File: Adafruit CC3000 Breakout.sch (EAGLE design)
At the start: 30 parts, among them U1 CC3000MOD, U3 74HC4050D, X1 2500AT44M0400E

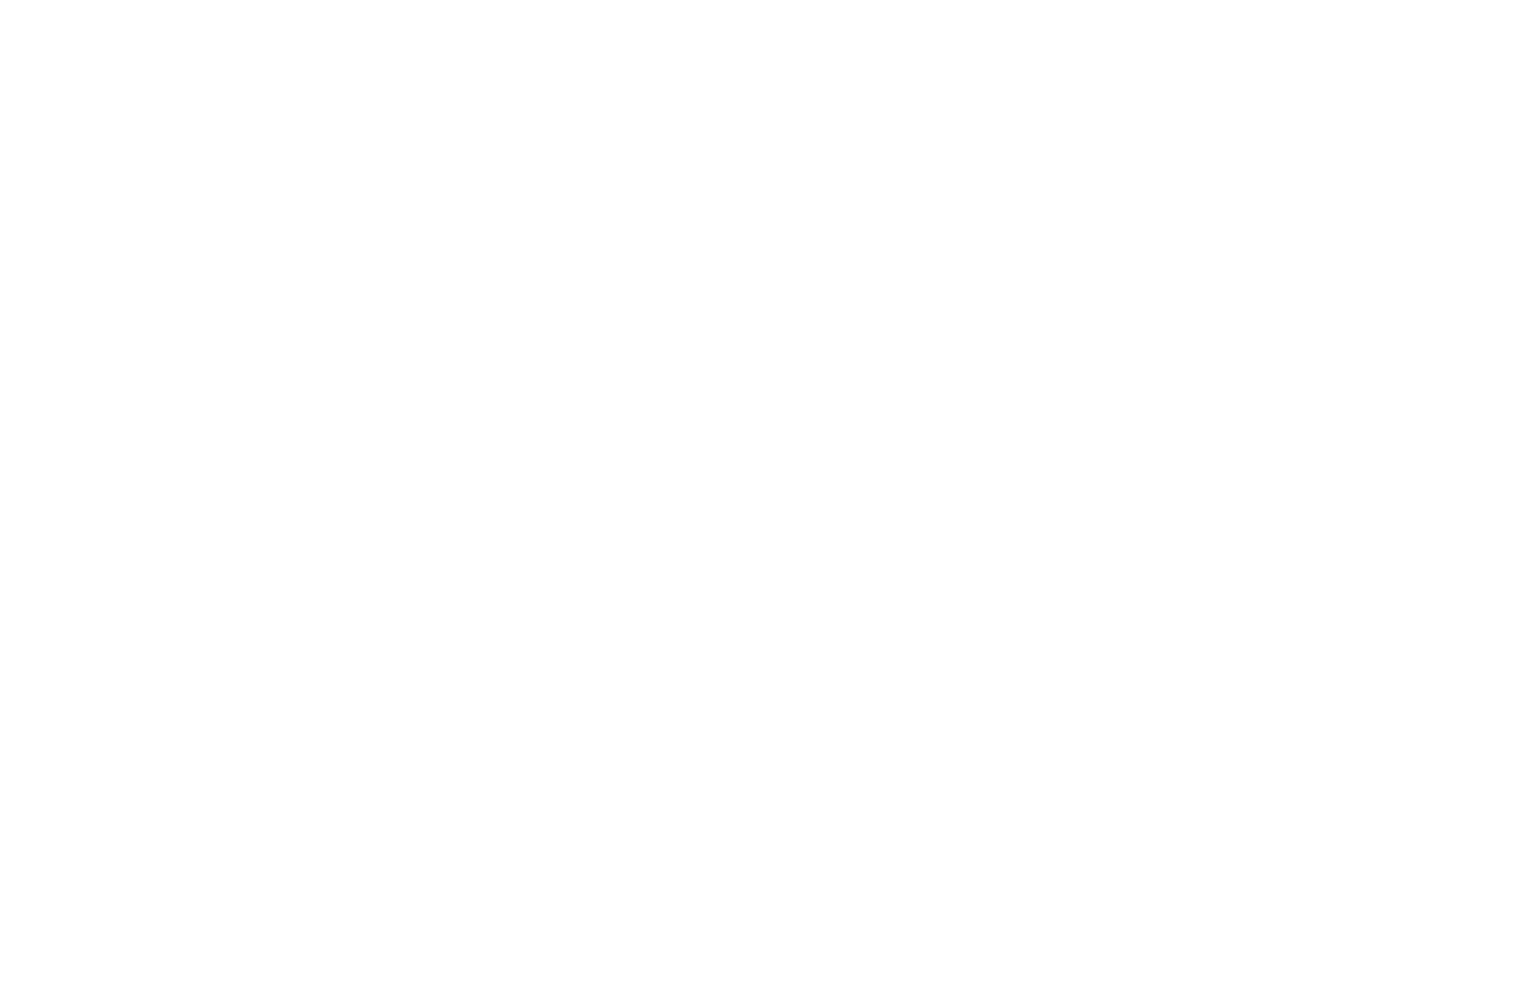
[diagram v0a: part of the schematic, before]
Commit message: Merge with net widget.
https://github.com/damellis/netwidget
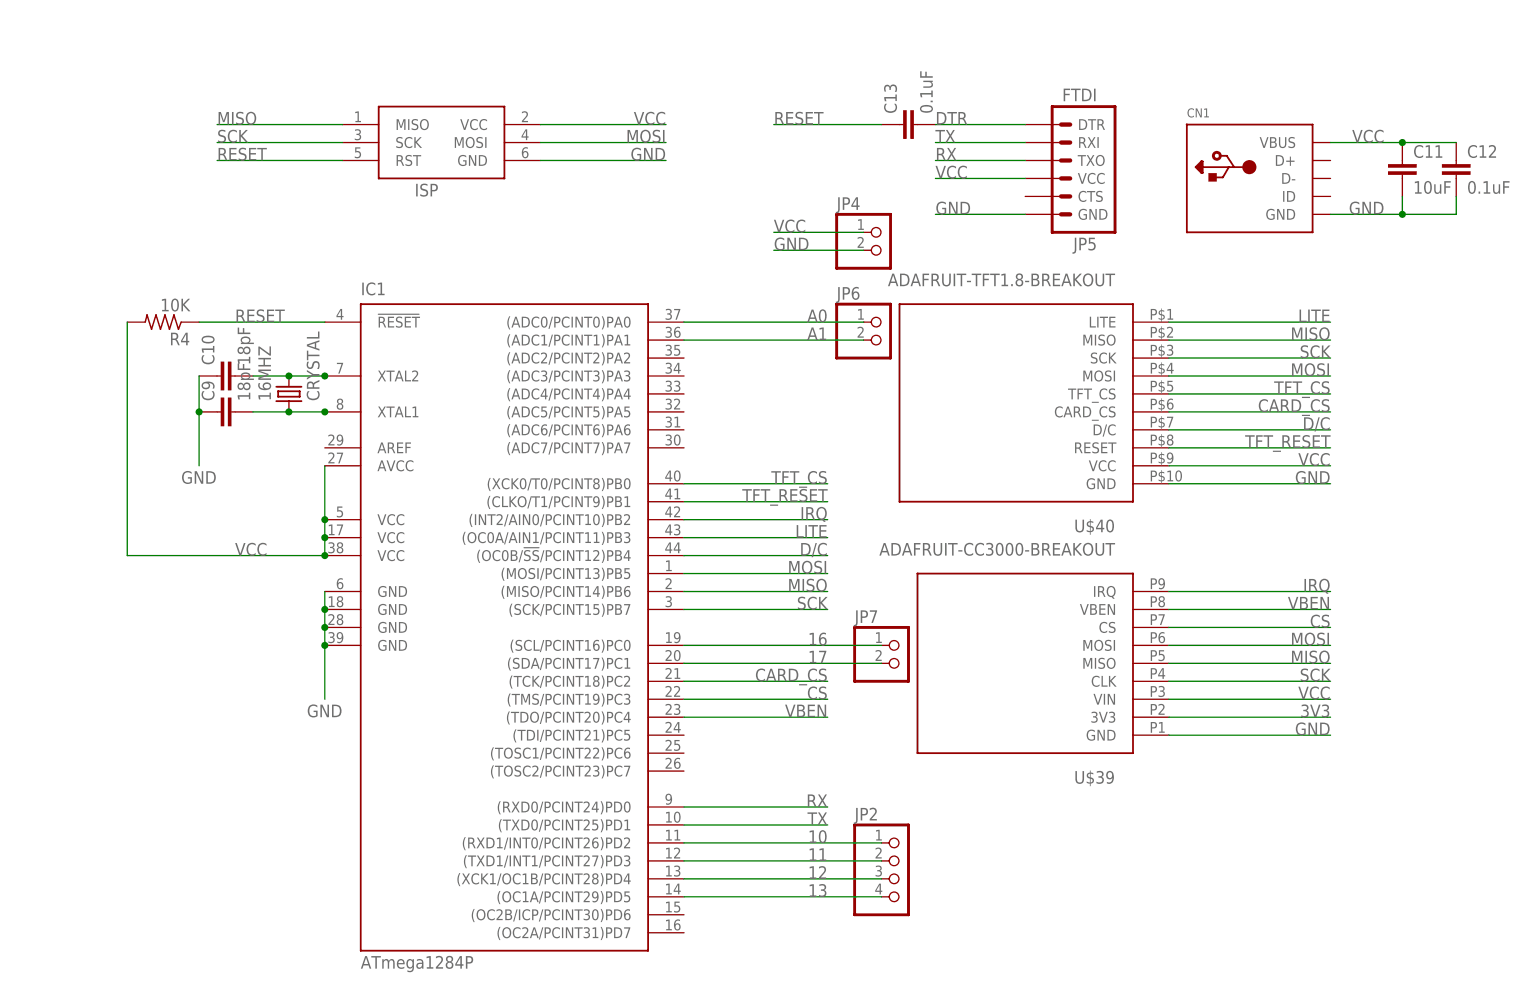
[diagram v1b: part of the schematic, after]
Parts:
- added 16MHZ: CRYSTAL, Net Widget:CRYSTAL
- added C10, C9: 18pF, rcl:C-EUC1206
- added C11: 10uF, rcl:C-EUC1206
- added C12, C13: 0.1uF, rcl:C-EUC1206
- added CN1: (no value), Net Widget:USBPWR
- added IC1: ATmega1284P, avr-5:MEGA164P/324P/644P-AU
- added ISP: AVRISP-6, adafruit:AVRISP-6
- added JP2: (no value), pinhead:PINHD-1X4
- added JP4, JP6, JP7: (no value), pinhead:PINHD-1X2
- added JP5: FTDI, Net Widget:ARDUINO_SERIAL_PROGRAMPTH
- added R4: 10K, rcl:R-US_R1206
- added U$39: ADAFRUIT-CC3000-BREAKOUT, Net Widget:ADAFRUIT-CC3000-BREAKOUT
- added U$40: ADAFRUIT-TFT1.8-BREAKOUT, Net Widget:ADAFRUIT-TFT1.8-BREAKOUT
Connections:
- new net 10: IC1.(RXD1/INT0/PCINT26)PD2, JP2.1
- new net 11: IC1.(TXD1/INT1/PCINT27)PD3, JP2.2
- new net 12: IC1.(XCK1/OC1B/PCINT28)PD4, JP2.3
- new net 13: IC1.(OC1A/PCINT29)PD5, JP2.4
- new net 16: IC1.(SCL/PCINT16)PC0, JP7.1
- new net 17: IC1.(SDA/PCINT17)PC1, JP7.2
- new net 3V3: U$39.3V3
- new net A0: IC1.(ADC0/PCINT0)PA0, JP6.1
- new net A1: IC1.(ADC1/PCINT1)PA1, JP6.2
- new net CARD_CS: IC1.(TCK/PCINT18)PC2, U$40.CARD_CS
- new net CS: IC1.(TMS/PCINT19)PC3, U$39.CS
- new net D/C: IC1.(OC0B/!SS!/PCINT12)PB4, U$40.D/C
- new net DTR: C13.2, JP5.DTR
- new net IRQ: IC1.(INT2/AIN0/PCINT10)PB2, U$39.IRQ
- new net LITE: IC1.(OC0A/AIN1/PCINT11)PB3, U$40.LITE
- new net MISO: IC1.(MISO/PCINT14)PB6, ISP.MISO, U$39.MISO, U$40.MISO
- new net MOSI: IC1.(MOSI/PCINT13)PB5, ISP.MOSI, U$39.MOSI, U$40.MOSI
- new net N$10: 16MHZ.1, C9.2, IC1.XTAL1
- new net N$8: 16MHZ.2, C10.2, IC1.XTAL2
- new net RESET: C13.1, IC1.!RESET, ISP.RST, R4.1
- new net RX: IC1.(RXD0/PCINT24)PD0, JP5.TXO
- new net SCK: IC1.(SCK/PCINT15)PB7, ISP.SCK, U$39.CLK, U$40.SCK
- new net TFT_CS: IC1.(XCK0/T0/PCINT8)PB0, U$40.TFT_CS
- new net TFT_RESET: IC1.(CLKO/T1/PCINT9)PB1, U$40.RESET
- new net TX: IC1.(TXD0/PCINT25)PD1, JP5.RXI
- new net VBEN: IC1.(TDO/PCINT20)PC4, U$39.VBEN
- new net VCC: C11.1, C12.1, CN1.VBUS, IC1.AVCC, IC1.VCC@1, IC1.VCC@2, IC1.VCC@3, ISP.VCC, JP4.1, JP5.VCC, R4.2, U$39.VIN, U$40.VCC
- net GND: now also C10.1, C11.2, C12.2, C9.1, CN1.GND, IC1.GND@1, IC1.GND@2, IC1.GND@3, IC1.GND@4, ISP.GND, JP4.2, JP5.GND, U$39.GND, U$40.GND

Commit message: Smoosh everything together.
Not routed yet, and some passives are 1206 and others are 0805.
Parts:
- removed 16MHZ: CRYSTAL, Net Widget:CRYSTAL
- removed C12: 0.1uF, rcl:C-EUC1206
- removed JP2: (no value), pinhead:PINHD-1X4
- removed JP3: (no value), microbuilder:HEADER-1X970MIL
- removed JP4, JP6, JP7: (no value), pinhead:PINHD-1X2
- removed U$39: ADAFRUIT-CC3000-BREAKOUT, Net Widget:ADAFRUIT-CC3000-BREAKOUT
- removed U$40: ADAFRUIT-TFT1.8-BREAKOUT, Net Widget:ADAFRUIT-TFT1.8-BREAKOUT
- removed U3: 74HC4050D, microbuilder:74HC4050D
- added 8MHZ: CRYSTAL, Net Widget:CRYSTAL
- C11: value 10uF -> 0.1uF
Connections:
- removed net 3V3: U$39.3V3
- removed net CARD_CS: IC1.(TCK/PCINT18)PC2, U$40.CARD_CS
- removed net CS: IC1.(TMS/PCINT19)PC3, U$39.CS
- removed net D/C: IC1.(OC0B/!SS!/PCINT12)PB4, U$40.D/C
- removed net IRQ: IC1.(INT2/AIN0/PCINT10)PB2, U$39.IRQ
- removed net LITE: IC1.(OC0A/AIN1/PCINT11)PB3, U$40.LITE
- removed net MISO: IC1.(MISO/PCINT14)PB6, ISP.MISO, U$39.MISO, U$40.MISO
- removed net MOSI: IC1.(MOSI/PCINT13)PB5, ISP.MOSI, U$39.MOSI, U$40.MOSI
- removed net SCK: IC1.(SCK/PCINT15)PB7, ISP.SCK, U$39.CLK, U$40.SCK
- removed net SPI_CLK_5V: JP3.6, U3.4A
- removed net SPI_CS_5V: JP3.3, R3.2, U3.6A
- removed net SPI_MOSI_5V: JP3.4, U3.5A
- removed net TFT_CS: IC1.(XCK0/T0/PCINT8)PB0, U$40.TFT_CS
- removed net TFT_RESET: IC1.(CLKO/T1/PCINT9)PB1, U$40.RESET
- removed net VBAT_EN_5V: JP3.2, R2.2, U3.3A
- removed net VBEN: IC1.(TDO/PCINT20)PC4, U$39.VBEN
- removed net VCC: C11.1, C12.1, CN1.VBUS, IC1.AVCC, IC1.VCC@1, IC1.VCC@2, IC1.VCC@3, ISP.VCC, JP4.1, JP5.VCC, R4.2, U$39.VIN, U$40.VCC
- net 10: no longer JP2.1
- net 11: no longer JP2.2
- net 12: no longer JP2.3
- net 13: no longer JP2.4
- net 16: no longer JP7.1
- net 17: no longer JP7.2
- net A0: no longer JP6.1
- net A1: no longer JP6.2
- net GND: no longer C12.2, JP3.9, JP4.2, U$39.GND, U$40.GND, U3.GND
- net N$10: now also 8MHZ.1; no longer 16MHZ.1
- net N$8: now also 8MHZ.2; no longer 16MHZ.2
- net SPI_CLK_3V: now also IC1.(SCK/PCINT15)PB7, ISP.SCK; no longer U3.4Y
- net SPI_CS_3V: now also IC1.(TMS/PCINT19)PC3, R3.2; no longer U3.6Y
- net SPI_IRQ_3V: now also IC1.(INT2/AIN0/PCINT10)PB2; no longer JP3.1
- net SPI_MISO_3V: now also IC1.(MISO/PCINT14)PB6, ISP.MISO; no longer JP3.5
- net SPI_MOSI_3V: now also IC1.(MOSI/PCINT13)PB5, ISP.MOSI; no longer U3.5Y
- net VBAT: now also C11.1, IC1.AVCC, IC1.VCC@1, IC1.VCC@2, IC1.VCC@3, ISP.VCC, R4.2; no longer JP3.8, U3.VCC
- net VBAT_EN_3V: now also IC1.(TDO/PCINT20)PC4, R2.2; no longer U3.3Y
- net VIN: now also CN1.VBUS, JP5.VCC; no longer JP3.7
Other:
- moved on the sheet: C10, C11, C13, C6, C7, C8, C9, CN1, FB1, IC1, ISP, JP5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

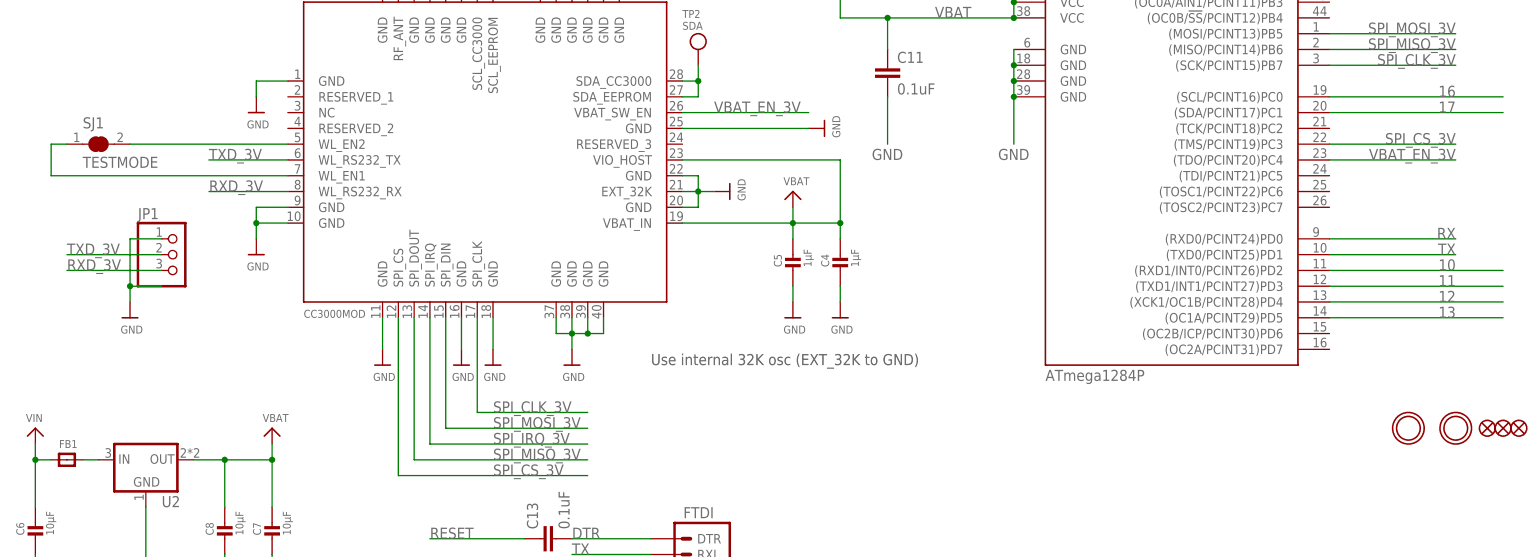
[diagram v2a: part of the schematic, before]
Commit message: Remove CC3000 RX and TX debug header.
And mounting holes.
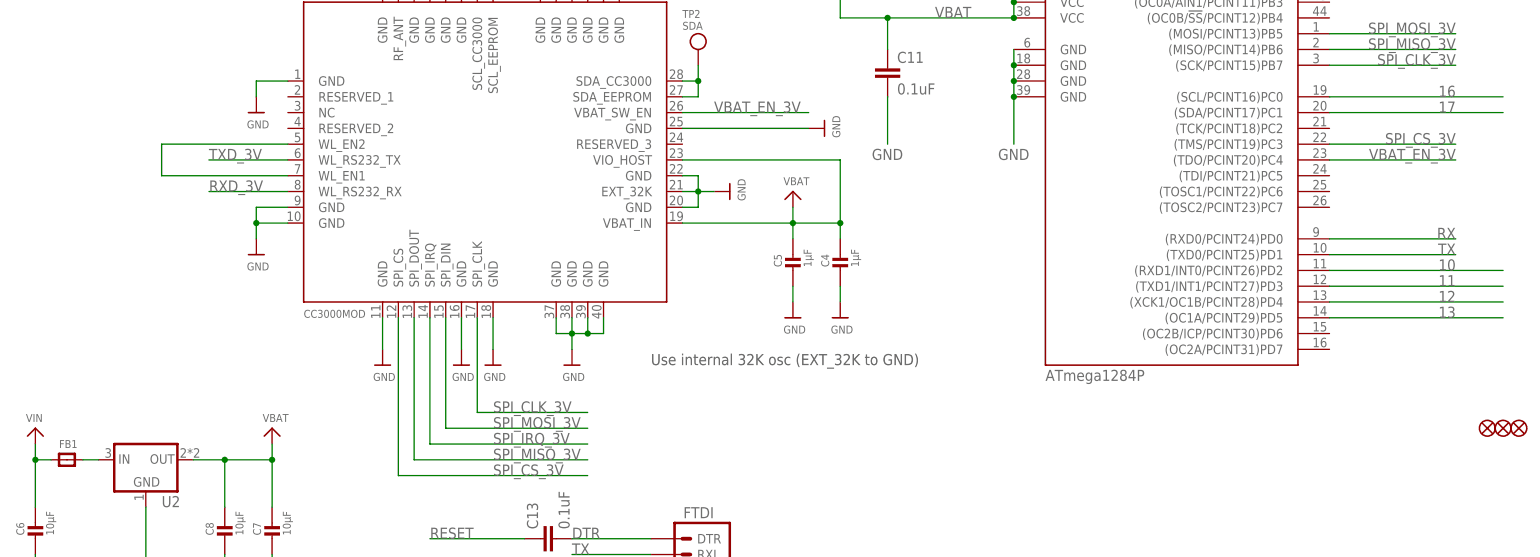
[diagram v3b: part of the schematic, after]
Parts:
- removed JP1: (no value), microbuilder:HEADER-1X3ROUND
- removed SJ1: TESTMODE, microbuilder:SOLDERJUMPER_CLOSED
- removed U$24, U$34: MOUNTINGHOLE2.5, microbuilder:MOUNTINGHOLE2.5
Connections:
- removed net N$5: SJ1.2, U1.WL_EN2
- net GND: no longer JP1.1
- net N$6: now also U1.WL_EN2; no longer SJ1.1
- net RXD_3V: no longer JP1.3
- net TXD_3V: no longer JP1.2
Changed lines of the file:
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@@
 <part name="U$18" library="microbuilder" deviceset="GND" device=""/>
 <part name="U$19" library="microbuilder" deviceset="GND" device=""/>
-<part name="SJ1" library="microbuilder" deviceset="SOLDERJUMPER_CLOSED" device="" value="TESTMODE"/>
 <part name="U$20" library="microbuilder" deviceset="GND" device=""/>
 <part name="FID1" library="microbuilder" deviceset="FIDUCIAL" device="&quot;&quot;"/>
@@
 <part name="R3" library="microbuilder" deviceset="RESISTOR" device="_0805MP" value="10K"/>
 <part name="U$22" library="microbuilder" deviceset="VBAT" device=""/>
-<part name="U$23" library="microbuilder" deviceset="GND" device=""/>
-<part name="U$24" library="microbuilder" deviceset="MOUNTINGHOLE" device="2.5"/>
-<part name="U$34" library="microbuilder" deviceset="MOUNTINGHOLE" device="2.5"/>
 <part name="U$35" library="microbuilder" deviceset="U.FL" device=""/>
 <part name="FID3" library="microbuilder" deviceset="FIDUCIAL" device="&quot;&quot;">
@@
 <part name="U$37" library="microbuilder" deviceset="GND" device=""/>
 <part name="U$38" library="microbuilder" deviceset="VBAT" device=""/>
-<part name="JP1" library="microbuilder" deviceset="HEADER-1X3" device="ROUND"/>
 <part name="ISP" library="adafruit" deviceset="AVRISP" device="-6"/>
 <part name="C9" library="rcl" deviceset="C-EU" device="C1206" value="18pF"/>
@@
 <instance part="U$18" gate="G$1" x="71.12" y="50.8"/>
 <instance part="U$19" gate="G$1" x="50.8" y="68.58"/>
-<instance part="SJ1" gate="G$1" x="25.4" y="86.36"/>
 <instance part="U$20" gate="G$1" x="50.8" y="91.44"/>
 <instance part="FID1" gate="G$1" x="254" y="40.64"/>
@@
 <instance part="R3" gate="G$1" x="124.46" y="142.24" rot="R270"/>
 <instance part="U$22" gate="G$1" x="124.46" y="154.94"/>
-<instance part="U$23" gate="G$1" x="30.48" y="58.42"/>
-<instance part="U$24" gate="G$1" x="243.84" y="40.64"/>
-<instance part="U$34" gate="G$1" x="236.22" y="40.64"/>
 <instance part="U$35" gate="G$1" x="55.88" y="129.54"/>
 <instance part="FID3" gate="G$1" x="251.46" y="40.64"/>
@@
 <instance part="U$37" gate="G$1" x="91.44" y="132.08"/>
 <instance part="U$38" gate="G$1" x="91.44" y="165.1"/>
-<instance part="JP1" gate="A" x="38.1" y="68.58"/>
 <instance part="ISP" gate="G$1" x="167.64" y="160.02"/>
 <instance part="C9" gate="G$1" x="157.48" y="127" rot="R90"/>
@@
 </segment>
 <segment>
-<pinref part="U$23" gate="G$1" pin="GND"/>
-<wire x1="35.56" y1="63.5" x2="30.48" y2="63.5" width="0.1524" layer="91"/>
-<wire x1="30.48" y1="63.5" x2="30.48" y2="60.96" width="0.1524" layer="91"/>
-<wire x1="30.48" y1="63.5" x2="30.48" y2="71.12" width="0.1524" layer="91"/>
-<junction x="30.48" y="63.5"/>
-<pinref part="JP1" gate="A" pin="1"/>
-<wire x1="30.48" y1="71.12" x2="35.56" y2="71.12" width="0.1524" layer="91"/>
-</segment>
-<segment>
 <pinref part="U$37" gate="G$1" pin="GND"/>
 <pinref part="R1" gate="G$1" pin="1"/>
@@
 </segment>
 </net>
-<net name="N$5" class="0">
-<segment>
+<net name="N$6" class="0">
+<segment>
+<pinref part="U1" gate="G$1" pin="WL_EN1"/>
+<wire x1="55.88" y1="81.28" x2="35.56" y2="81.28" width="0.1524" layer="91"/>
+<wire x1="35.56" y1="81.28" x2="35.56" y2="86.36" width="0.1524" layer="91"/>
 <pinref part="U1" gate="G$1" pin="WL_EN2"/>
-<pinref part="SJ1" gate="G$1" pin="2"/>
-<wire x1="55.88" y1="86.36" x2="30.48" y2="86.36" width="0.1524" layer="91"/>
-</segment>
-</net>
-<net name="N$6" class="0">
-<segment>
-<pinref part="U1" gate="G$1" pin="WL_EN1"/>
-<wire x1="55.88" y1="81.28" x2="17.78" y2="81.28" width="0.1524" layer="91"/>
-<wire x1="17.78" y1="81.28" x2="17.78" y2="86.36" width="0.1524" layer="91"/>
-<pinref part="SJ1" gate="G$1" pin="1"/>
-<wire x1="17.78" y1="86.36" x2="20.32" y2="86.36" width="0.1524" layer="91"/>
+<wire x1="55.88" y1="86.36" x2="35.56" y2="86.36" width="0.1524" layer="91"/>
 </segment>
 </net>
@@
 <wire x1="55.88" y1="78.74" x2="43.18" y2="78.74" width="0.1524" layer="91"/>
 <label x="43.18" y="78.74" size="1.778" layer="95"/>
-<wire x1="35.56" y1="66.04" x2="20.32" y2="66.04" width="0.1524" layer="91"/>
-<label x="20.32" y="66.04" size="1.778" layer="95"/>
-<pinref part="JP1" gate="A" pin="3"/>
 </segment>
 </net>
@@
 <wire x1="55.88" y1="83.82" x2="43.18" y2="83.82" width="0.1524" layer="91"/>
 <label x="43.18" y="83.82" size="1.778" layer="95"/>
-<wire x1="35.56" y1="68.58" x2="20.32" y2="68.58" width="0.1524" layer="91"/>
-<label x="20.32" y="68.58" size="1.778" layer="95"/>
-<pinref part="JP1" gate="A" pin="2"/>
-</segment>
-</net>
+</segment>
+</net>
